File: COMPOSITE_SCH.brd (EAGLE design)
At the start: 43.5 x 28 mm, 10 parts, among them J1 RCALOCK, T1 BC337

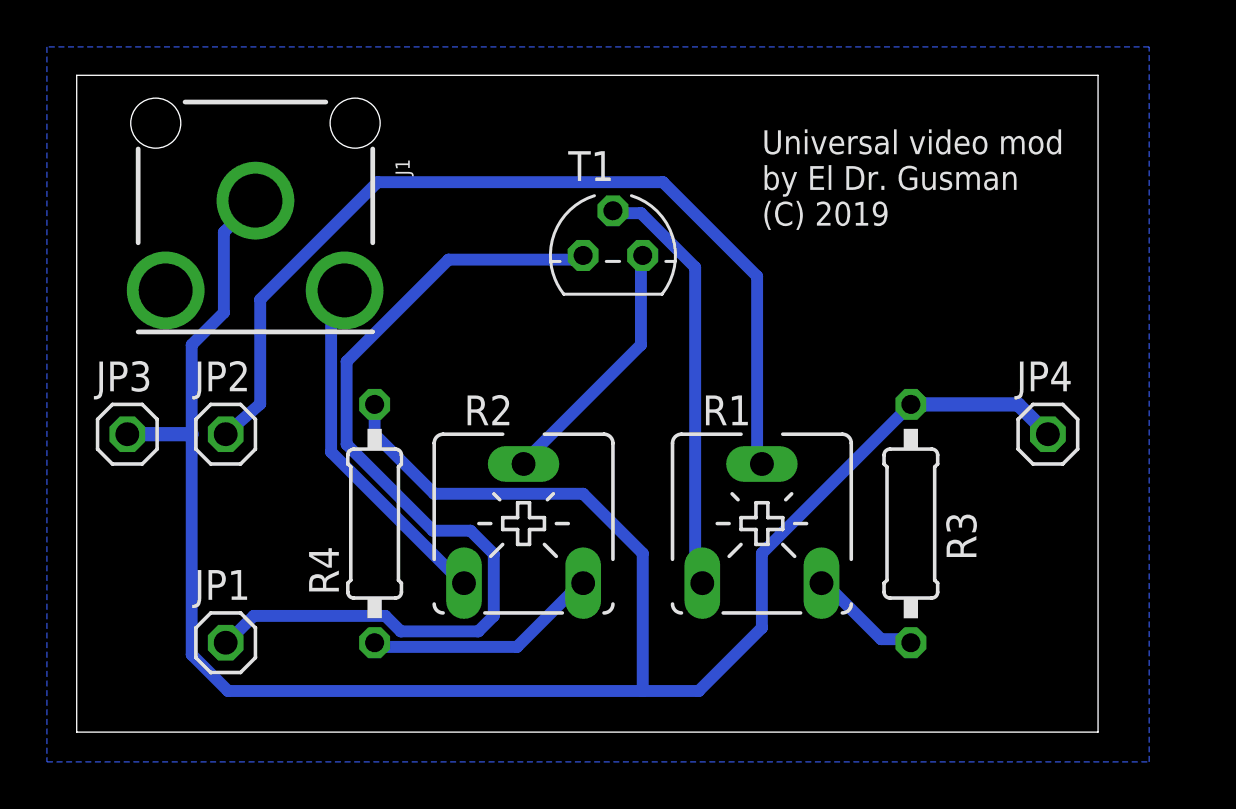
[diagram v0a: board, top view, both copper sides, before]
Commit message: Updated design to improve video quality
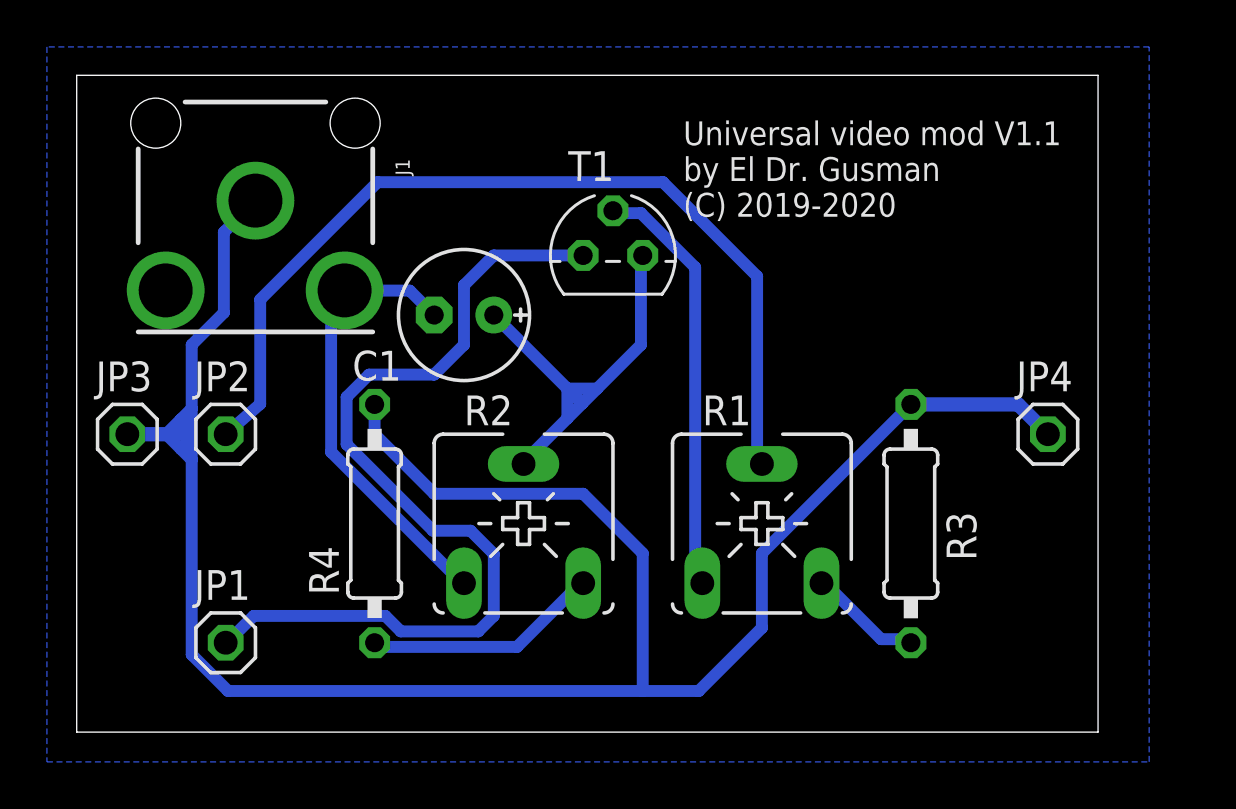
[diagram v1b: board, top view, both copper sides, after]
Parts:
- added C1: 100uF 10v, rcl:E2,5-6E
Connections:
- net N$3: now also C1.+
- net N$6: now also C1.-
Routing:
- net N$3: track 11.0 -> 18.8 mm
- net GND: track 88.8 -> 93.3 mm
- net N$6: track 15.2 -> 19.7 mm
- net VCC: track 38.8 -> 39.4 mm
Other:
- board text added: "Universal video mod V1.1 by El Dr. Gusman (C) 2019-2020"
- board text removed: "Universal video mod by El Dr. Gusman (C) 2019"
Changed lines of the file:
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@@
 <drawing>
 <settings>
-<setting alwaysvectorfont="no"/>
+<setting alwaysvectorfont="yes"/>
 <setting verticaltext="up"/>
 </settings>
-<grid distance="50" unitdist="mil" unit="mil" style="lines" multiple="1" display="no" altdistance="5" altunitdist="mil" altunit="mil"/>
+<grid distance="1" unitdist="mil" unit="mil" style="lines" multiple="1" display="no" altdistance="5" altunitdist="mil" altunit="mil"/>
 <layers>
 <layer number="1" name="Top" color="4" fill="1" visible="yes" active="yes"/>
@@
 <wire x1="42.26991875" y1="27.99994375" x2="-1.27" y2="27.99994375" width="0" layer="20"/>
 <wire x1="-1.27" y1="27.99994375" x2="-1.27" y2="0" width="0" layer="20"/>
-<text x="27.94" y="21.59" size="1.016" layer="25">Universal video mod
+<text x="24.5872" y="21.971" size="1.016" layer="25">Universal video mod V1.1
 by El Dr. Gusman
-(C) 2019</text>
+(C) 2019-2020</text>
 <dimension x1="42.26991875" y1="27.99994375" x2="-1.27" y2="27.99994375" x3="20.499959375" y3="34.29" textsize="1.778" layer="25"/>
 <dimension x1="-1.27" y1="27.99994375" x2="-1.27" y2="0" x3="-8.89" y3="13.999971875" textsize="1.778" layer="25"/>
@@
 <attribute name="VALUE" x="19.685" y="16.51" size="1.27" layer="27" ratio="10"/>
 </element>
+<element name="C1" library="rcl" library_urn="urn:adsk.eagle:library:334" package="E2,5-6E" package3d_urn="urn:adsk.eagle:package:23430/1" value="100uF 10v" x="15.24" y="17.78" smashed="yes" rot="R180">
+<attribute name="NAME" x="12.573" y="16.256" size="1.27" layer="25" ratio="10" rot="R180"/>
+<attribute name="SPICEPREFIX" value="C" x="15.24" y="17.78" size="1.778" layer="27" rot="R180" display="off"/>
+<attribute name="VALUE" x="12.573" y="20.32" size="1.27" layer="27" ratio="10" rot="R180"/>
+</element>
 </elements>
 <signals>
@@
 <contactref element="R2" pad="S"/>
 <wire x1="22.7838" y1="16.51" x2="22.7838" y2="20.1422" width="0.508" layer="16"/>
-<wire x1="17.8308" y1="11.557" x2="22.7838" y2="16.51" width="0.508" layer="16"/>
+<wire x1="17.8308" y1="11.557" x2="19.6469" y2="13.3731" width="0.508" layer="16"/>
+<wire x1="19.6469" y1="13.3731" x2="20.2819" y2="14.0081" width="0.508" layer="16"/>
+<wire x1="20.2819" y1="14.0081" x2="20.9169" y2="14.6431" width="0.508" layer="16"/>
+<wire x1="20.9169" y1="14.6431" x2="22.7838" y2="16.51" width="0.508" layer="16"/>
 <wire x1="22.7838" y1="20.1422" x2="22.86" y2="20.32" width="0.508" layer="16"/>
 <wire x1="17.8308" y1="11.557" x2="17.78" y2="11.43" width="0.508" layer="16"/>
+<contactref element="C1" pad="+"/>
+<wire x1="16.51" y1="17.78" x2="19.6469" y2="14.6431" width="0.508" layer="16"/>
+<wire x1="19.6469" y1="14.6431" x2="20.2819" y2="14.0081" width="0.508" layer="16"/>
+<wire x1="19.6469" y1="14.6431" x2="19.6469" y2="13.3731" width="0.508" layer="16"/>
+<wire x1="19.6469" y1="14.6431" x2="20.9169" y2="14.6431" width="0.508" layer="16"/>
 </signal>
 <signal name="N$4">
@@
 <wire x1="9.906" y1="18.8214" x2="9.5758" y2="18.4912" width="0.508" layer="16"/>
 <wire x1="9.906" y1="18.8214" x2="10.1516" y2="18.8298" width="0.508" layer="16"/>
+<contactref element="C1" pad="-"/>
+<wire x1="13.97" y1="17.78" x2="12.9286" y2="18.8214" width="0.508" layer="16"/>
+<wire x1="12.9286" y1="18.8214" x2="9.906" y2="18.8214" width="0.508" layer="16"/>
 </signal>
 <signal name="N$8">
@@
 <contactref element="JP1" pad="1"/>
 <contactref element="T1" pad="3"/>
-<wire x1="14.5796" y1="20.1422" x2="20.1422" y2="20.1422" width="0.508" layer="16"/>
-<wire x1="10.2362" y1="15.7988" x2="14.5796" y2="20.1422" width="0.508" layer="16"/>
-<wire x1="10.2362" y1="12.2682" x2="10.2362" y2="15.7988" width="0.508" layer="16"/>
+<wire x1="10.2362" y1="12.2682" x2="10.2362" y2="14.2848875" width="0.508" layer="16"/>
 <wire x1="13.9192" y1="8.5852" x2="10.2362" y2="12.2682" width="0.508" layer="16"/>
 <wire x1="15.5194" y1="8.5852" x2="13.9192" y2="8.5852" width="0.508" layer="16"/>
@@
 <wire x1="6.2738" y1="4.953" x2="11.8872" y2="4.953" width="0.508" layer="16"/>
 <wire x1="5.2832" y1="3.9624" x2="6.2738" y2="4.953" width="0.508" layer="16"/>
-<wire x1="20.1422" y1="20.1422" x2="20.32" y2="20.32" width="0.508" layer="16"/>
 <wire x1="5.2832" y1="3.9624" x2="5.08" y2="3.81" width="0.508" layer="16"/>
+<wire x1="20.32" y1="20.32" x2="16.51" y2="20.32" width="0.508" layer="16"/>
+<wire x1="16.51" y1="20.32" x2="15.24" y2="19.05" width="0.508" layer="16"/>
+<wire x1="15.24" y1="19.05" x2="15.24" y2="16.51" width="0.508" layer="16"/>
+<wire x1="15.24" y1="16.51" x2="13.97" y2="15.24" width="0.508" layer="16"/>
+<wire x1="11.1913125" y1="15.24" x2="10.2362" y2="14.2848875" width="0.508" layer="16"/>
+<wire x1="13.97" y1="15.24" x2="11.1913125" y2="15.24" width="0.508" layer="16"/>
 </signal>
 <signal name="GND">
@@
 <contactref element="JP4" pad="1"/>
 <contactref element="J1" pad="SHELL"/>
-<wire x1="34.0106" y1="13.8684" x2="34.29" y2="13.97" width="0.508" layer="16"/>
 <wire x1="5.0038" y1="17.8816" x2="5.0038" y2="21.3106" width="0.508" layer="16"/>
 <wire x1="3.6322" y1="16.51" x2="5.0038" y2="17.8816" width="0.508" layer="16"/>
-<wire x1="3.6322" y1="3.302" x2="3.6322" y2="12.7" width="0.508" layer="16"/>
-<wire x1="3.6322" y1="12.7" x2="3.6322" y2="16.51" width="0.508" layer="16"/>
+<wire x1="3.6322" y1="3.302" x2="3.6322" y2="11.6078" width="0.508" layer="16"/>
+<wire x1="3.6322" y1="11.6078" x2="3.6322" y2="12.5222" width="0.508" layer="16"/>
+<wire x1="3.6322" y1="12.5222" x2="3.6322" y2="13.7922" width="0.508" layer="16"/>
+<wire x1="3.6322" y1="13.7922" x2="3.6322" y2="16.51" width="0.508" layer="16"/>
 <wire x1="5.1816" y1="1.7526" x2="3.6322" y2="3.302" width="0.508" layer="16"/>
 <wire x1="5.1816" y1="1.7526" x2="22.86" y2="1.7526" width="0.508" layer="16"/>
 <wire x1="22.86" y1="1.7526" x2="25.2476" y2="1.7526" width="0.508" layer="16"/>
 <wire x1="5.0038" y1="21.3106" x2="6.35" y2="22.6568" width="0.508" layer="16"/>
-<wire x1="0.889" y1="12.7" x2="3.6322" y2="12.7" width="0.6096" layer="16"/>
+<wire x1="0.889" y1="12.7" x2="2.54" y2="12.7" width="0.6096" layer="16"/>
 <wire x1="40.132" y1="12.7" x2="38.862" y2="13.97" width="0.6096" layer="16"/>
 <wire x1="38.862" y1="13.97" x2="34.29" y2="13.97" width="0.6096" layer="16"/>
@@
 <vertex x="44.45" y="29.21"/>
 </polygon>
+<wire x1="3.175" y1="12.065" x2="3.6322" y2="11.6078" width="0.508" layer="16"/>
+<wire x1="3.6322" y1="12.5222" x2="3.175" y2="12.065" width="0.508" layer="16"/>
+<wire x1="3.175" y1="12.065" x2="2.54" y2="12.7" width="0.508" layer="16"/>
+<wire x1="3.6322" y1="13.7922" x2="3.175" y2="13.335" width="0.508" layer="16"/>
+<wire x1="3.175" y1="13.335" x2="2.54" y2="12.7" width="0.508" layer="16"/>
+<wire x1="2.54" y1="12.7" x2="3.4544" y2="12.7" width="0.508" layer="16"/>
+<wire x1="3.4544" y1="12.7" x2="3.6322" y2="12.5222" width="0.508" layer="16"/>
+<wire x1="3.6322" y1="12.5222" x2="3.6322" y2="12.8778" width="0.508" layer="16"/>
+<wire x1="3.6322" y1="12.8778" x2="3.175" y2="13.335" width="0.508" layer="16"/>
 </signal>
 </signals>
